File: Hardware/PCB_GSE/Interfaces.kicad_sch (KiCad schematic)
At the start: 16 parts, among them J1 GT17HN-4DP-2HA56, J15 Conn_01x02, J16 Conn_01x06_Pin, U5 ISOW1044

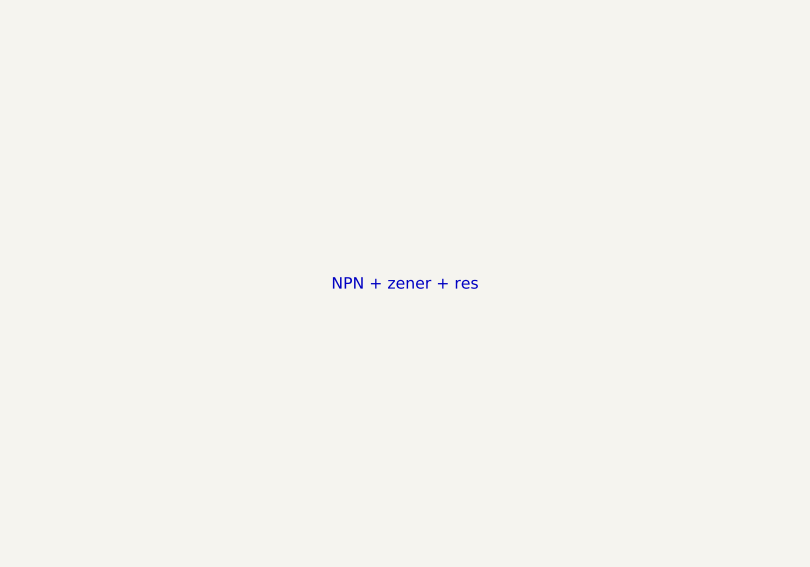
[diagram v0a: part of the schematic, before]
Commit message: fix: typos
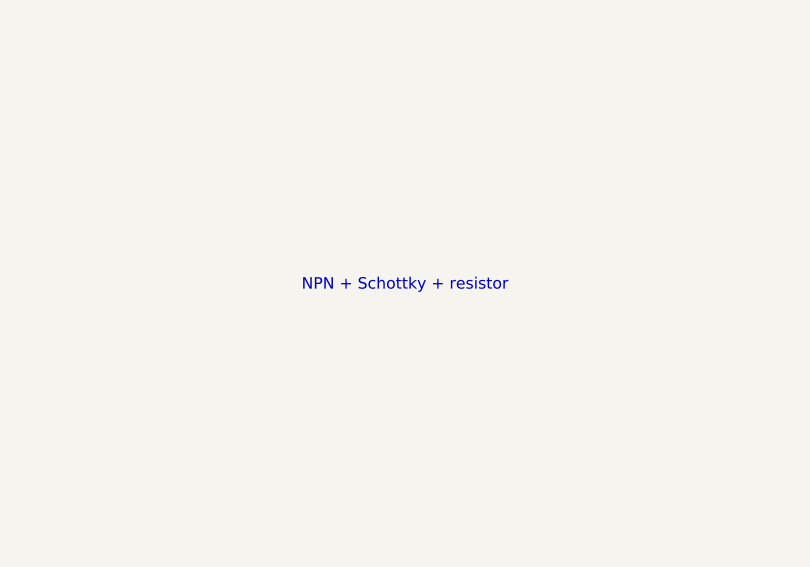
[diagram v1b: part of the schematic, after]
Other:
- note added: "NPN + Schottky + resistor"
- note removed: "NPN + zener + res"
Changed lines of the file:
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@@
 		)
 	)
-	(text "NPN + zener + res"
+	(text "NPN + Schottky + resistor"
 		(exclude_from_sim no)
 		(at 79.248 68.834 0)

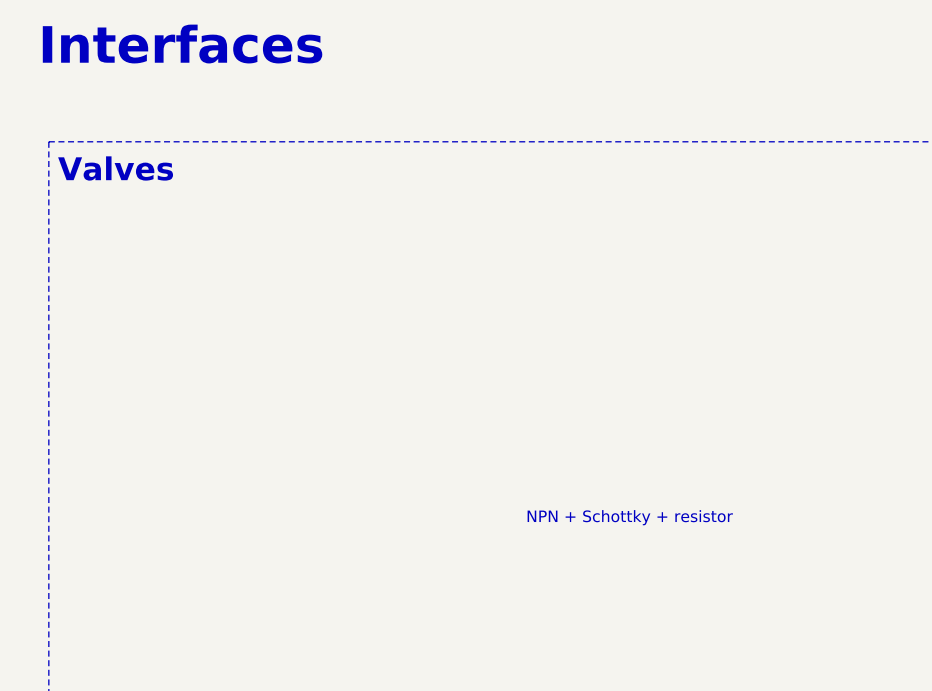
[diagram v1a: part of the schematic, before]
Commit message: fix: change Schottky diode 12v buck
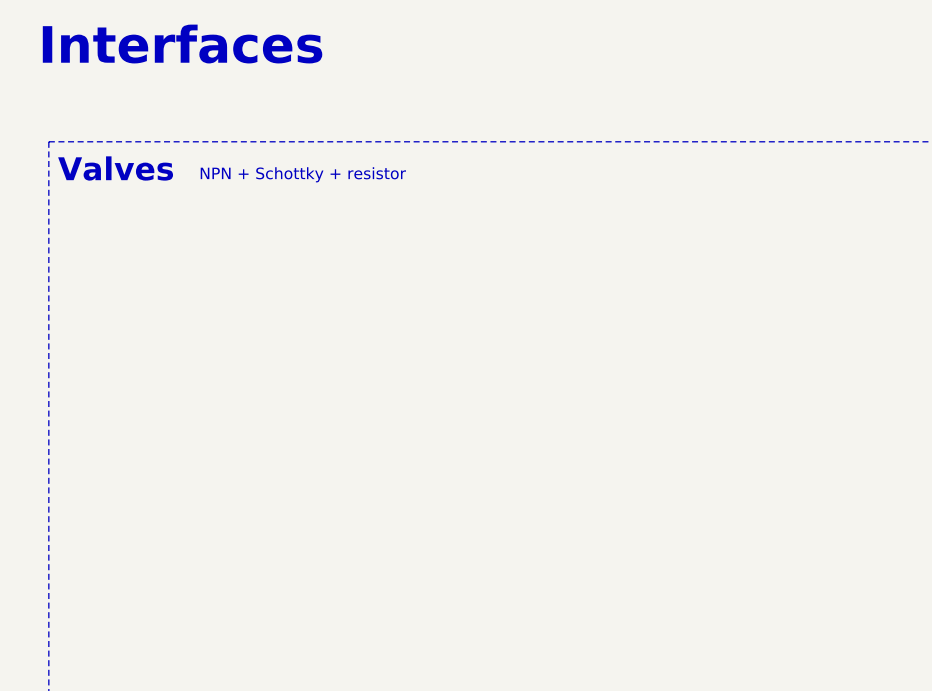
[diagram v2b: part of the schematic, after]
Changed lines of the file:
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@@
 	(text "NPN + Schottky + resistor"
 		(exclude_from_sim no)
-		(at 79.248 68.834 0)
+		(at 42.926 30.734 0)
 		(effects
 			(font

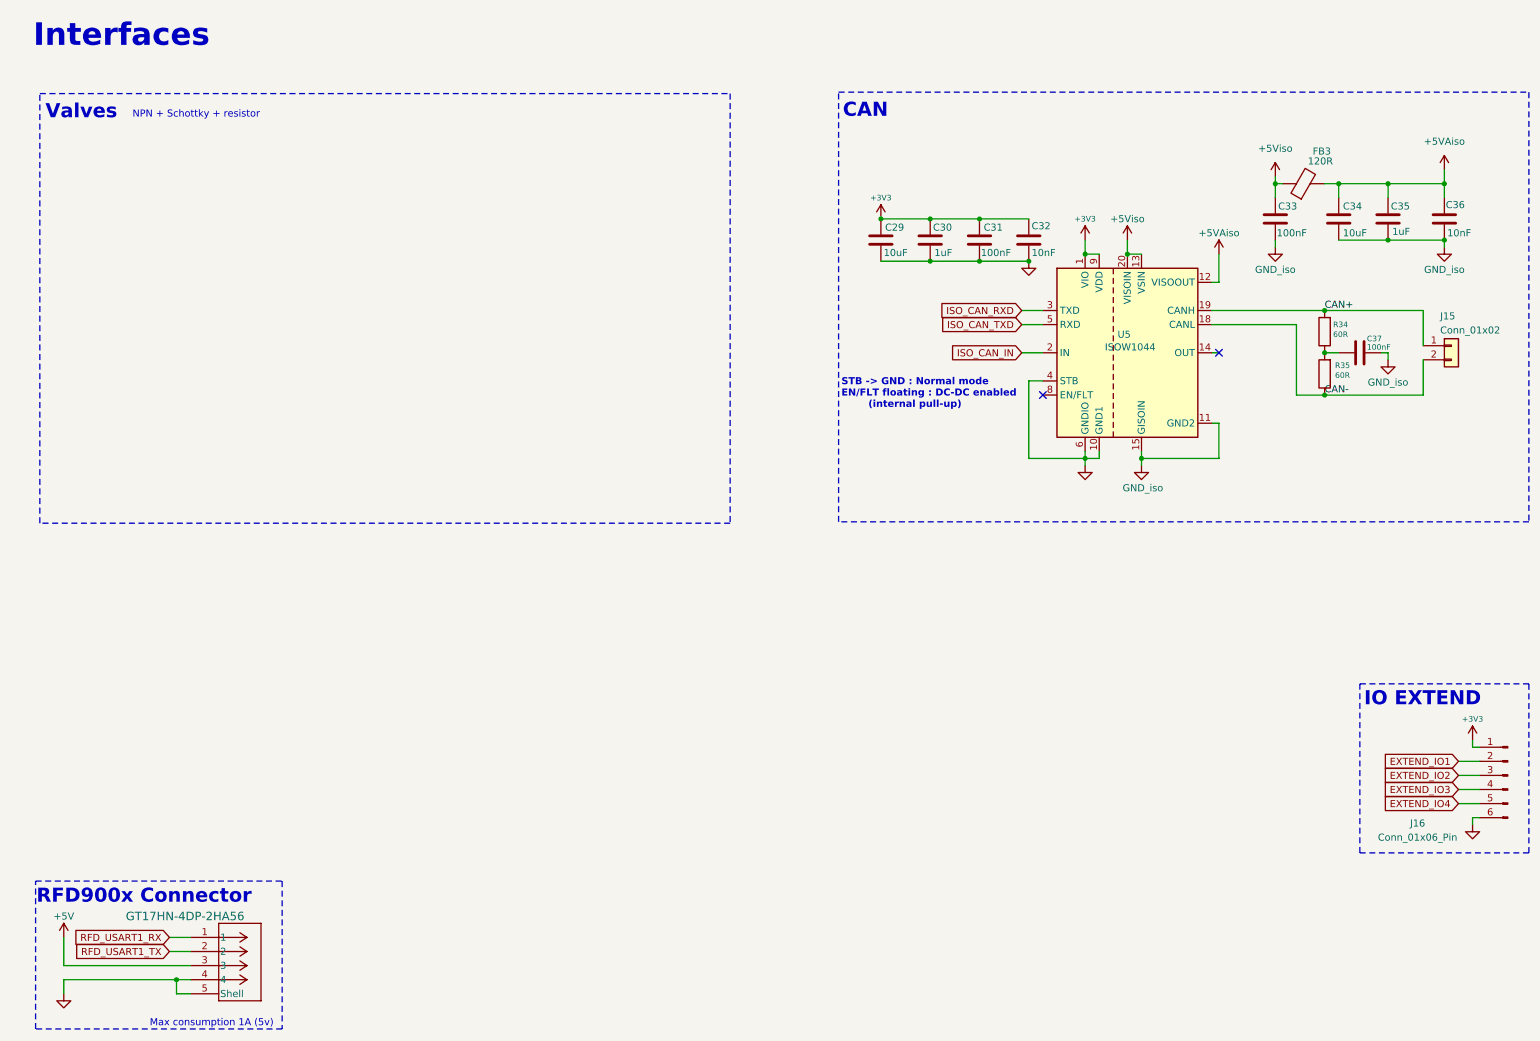
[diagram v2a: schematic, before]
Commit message: feat: add valve control + needed components
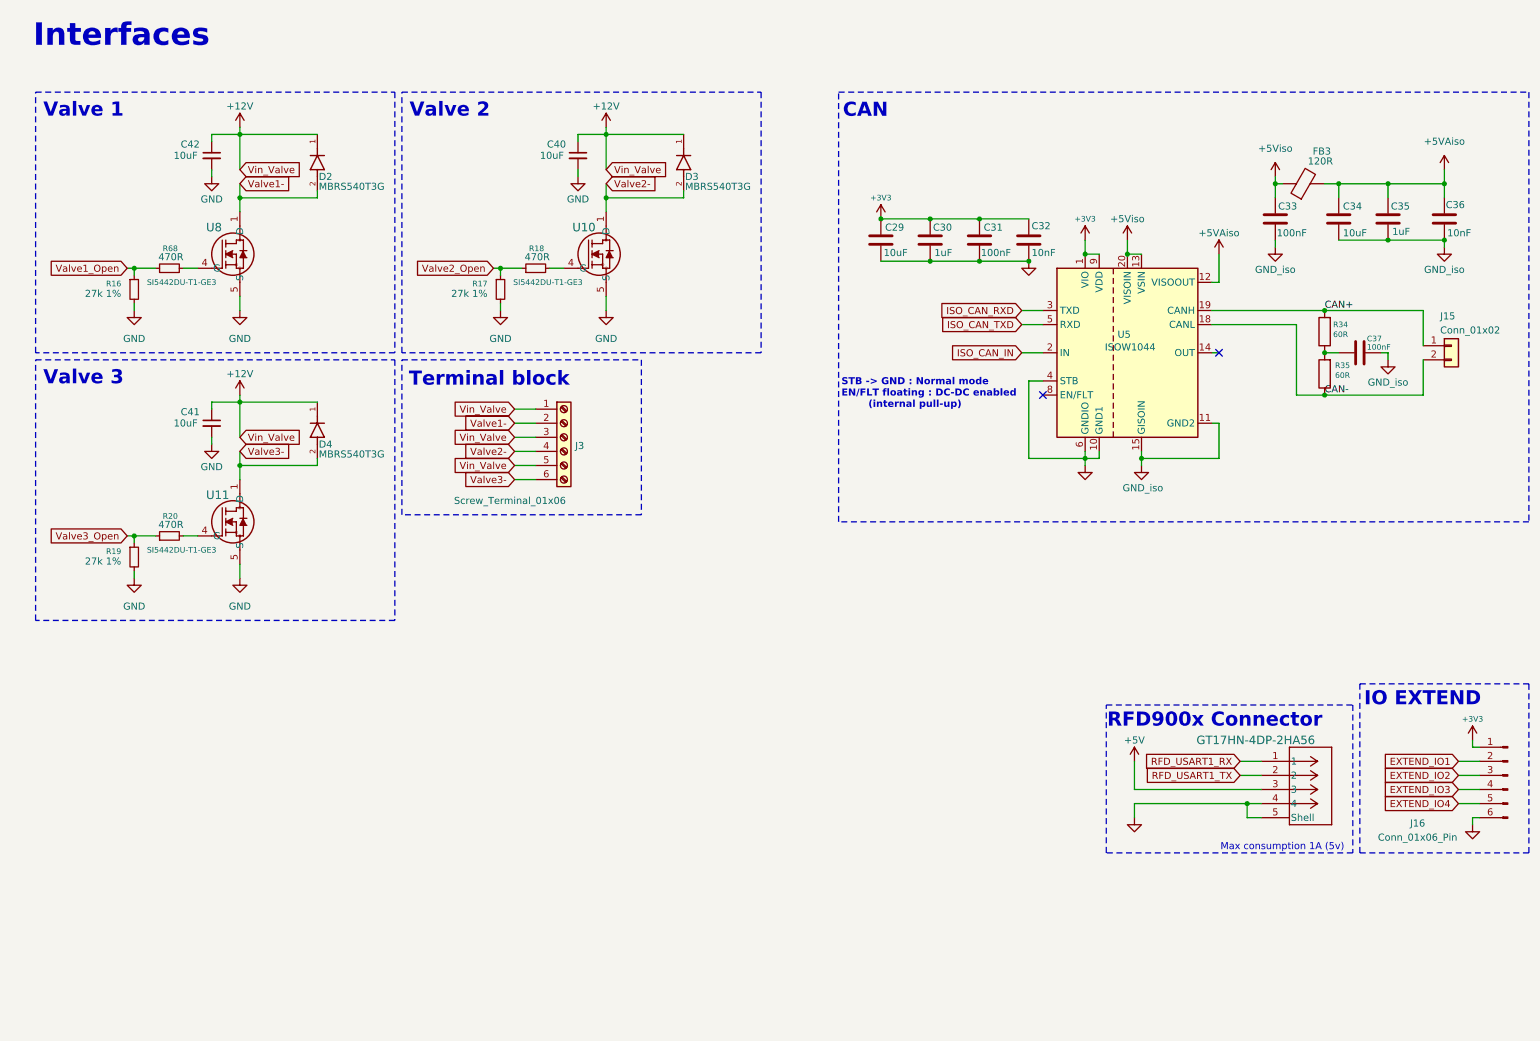
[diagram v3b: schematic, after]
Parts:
- added C40, C41, C42: 10uF, Capacitor_SMD:C_0603_1608Metric, symbol Device:C_Small
- added D2, D3, D4: MBRS540T3G, MBRS540T3G:DIOM7959X261N, symbol PCB_GSE:MBRS540T3G
- added J3: Screw_Terminal_01x06, symbol Connector:Screw_Terminal_01x06
- added R16, R17, R19: 27k 1%, Resistor_SMD:R_0603_1608Metric, symbol Device:R_Small
- added R18, R20, R68: 470R, Resistor_SMD:R_0603_1608Metric, symbol Device:R_Small
- added U10, U11, U8: SI5442DU-T1-GE3, symbol PCB_GSE:SI5442DU-T1-GE3
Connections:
- net GND: now also C40.2, C41.2, C42.2, R16.2, R17.2, R19.2, U10.5 (S), U10.9 (S), U11.5 (S), U11.9 (S), U8.5 (S), U8.9 (S)
- new net: R20.2, U11.4 (G)
- new net: R18.2, U10.4 (G)
- new net: R68.2, U8.4 (G)
- new net +12V: C40.1, C41.1, C42.1, D2.1, D3.1, D4.1, J3.1 (Pin_1), J3.3 (Pin_3), J3.5 (Pin_5)
- new net Valve1-: D2.2, J3.2 (Pin_2), U8.1 (D), U8.2 (D), U8.3 (D), U8.6 (D), U8.7 (D), U8.8 (D)
- new net Valve1_Open: R16.1, R68.1
- new net Valve2-: D3.2, J3.4 (Pin_4), U10.1 (D), U10.2 (D), U10.3 (D), U10.6 (D), U10.7 (D), U10.8 (D)
- new net Valve2_Open: R17.1, R18.1
- new net Valve3-: D4.2, J3.6 (Pin_6), U11.1 (D), U11.2 (D), U11.3 (D), U11.6 (D), U11.7 (D), U11.8 (D)
- new net Valve3_Open: R19.1, R20.1
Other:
- note added: "Terminal block"
- note added: "Valve 1"
- note added: "Valve 2"
- note added: "Valve 3"
- note removed: "NPN + Schottky + resistor"
- note removed: "Valves"

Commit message: feat: add extended ios + add stm32 project extended ios +
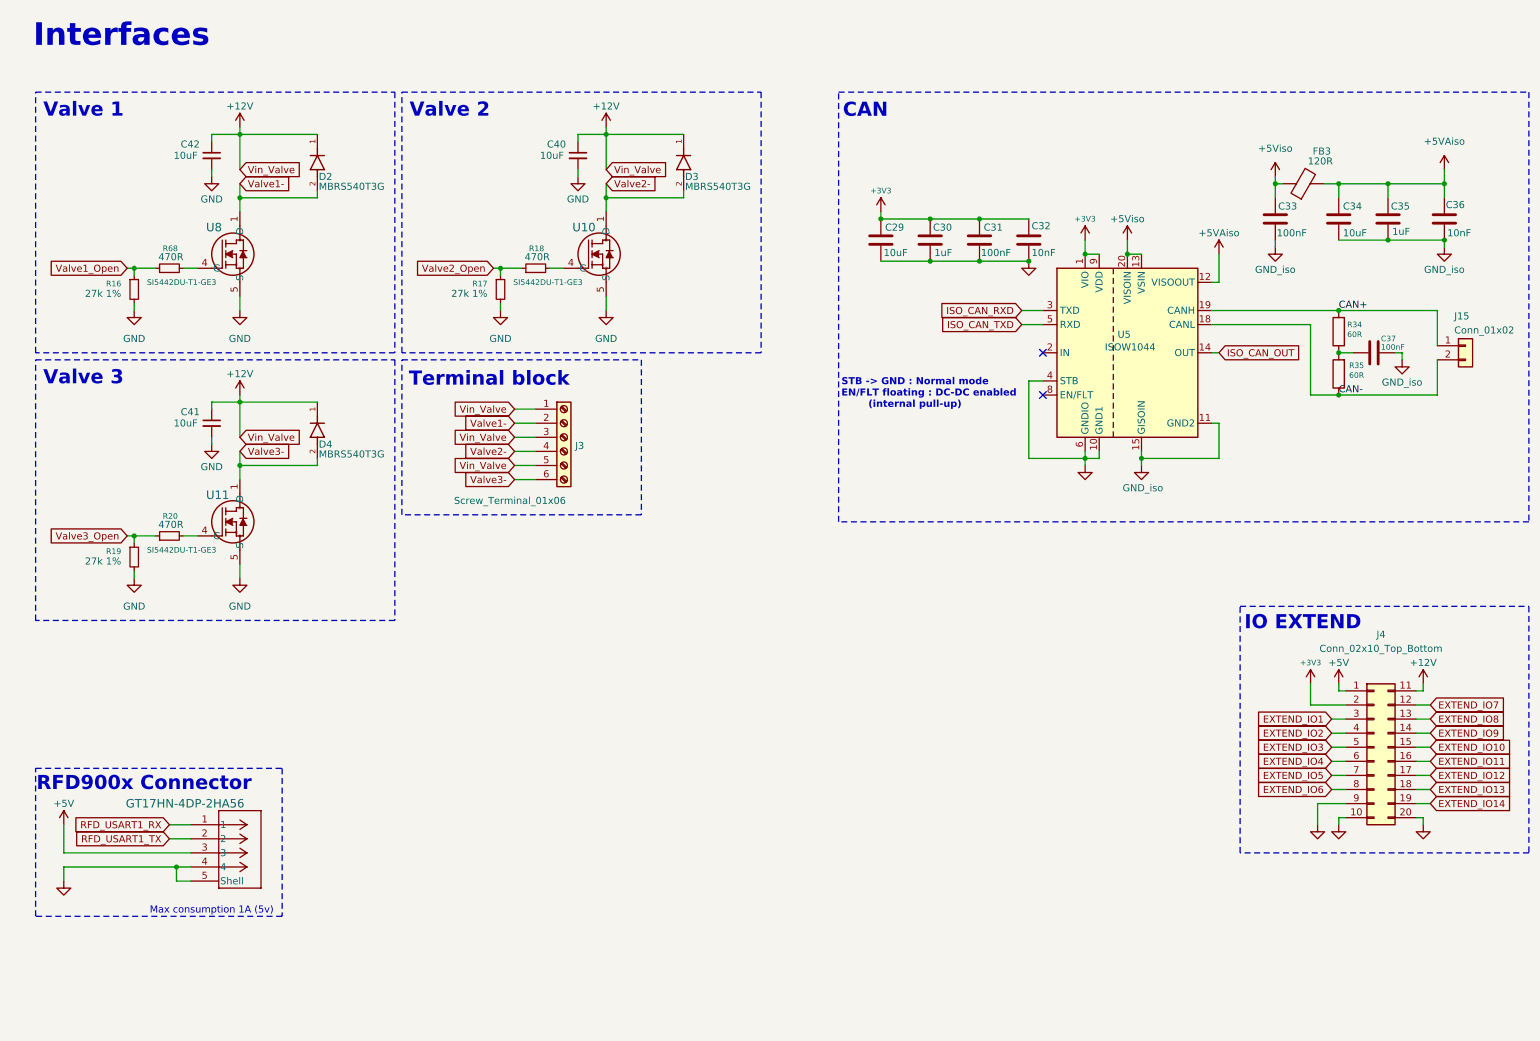
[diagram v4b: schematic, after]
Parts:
- removed J16: Conn_01x06_Pin, Connector_PinSocket_2.54mm:PinSocket_2x03_P2.54mm_Vertical, symbol Connector:Conn_01x06_Pin
- added J4: Conn_02x10_Top_Bottom, Connector_PinHeader_2.54mm:PinHeader_2x10_P2.54mm_Vertical, symbol Connector_Generic:Conn_02x10_Top_Bottom
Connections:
- net +12V: now also J4.11 (Pin_11)
- net +3V3: now also J4.2 (Pin_2)
- net +5V: now also J4.1 (Pin_1)
- net EXTEND_IO1: now also J4.3 (Pin_3)
- net EXTEND_IO2: now also J4.4 (Pin_4)
- net EXTEND_IO3: now also J4.5 (Pin_5)
- net EXTEND_IO4: now also J4.6 (Pin_6)
- net GND: now also J4.10 (Pin_10), J4.20 (Pin_20), J4.9 (Pin_9)
- net ISO_CAN_OUT: now reaches U5.14 (OUT)
- net ISO_CAN_IN: no longer names the net of U5.2 (IN)
- new net EXTEND_IO10: J4.15 (Pin_15)
- new net EXTEND_IO11: J4.16 (Pin_16)
- new net EXTEND_IO12: J4.17 (Pin_17)
- new net EXTEND_IO13: J4.18 (Pin_18)
- new net EXTEND_IO14: J4.19 (Pin_19)
- new net EXTEND_IO5: J4.7 (Pin_7)
- new net EXTEND_IO6: J4.8 (Pin_8)
- new net EXTEND_IO7: J4.12 (Pin_12)
- new net EXTEND_IO8: J4.13 (Pin_13)
- new net EXTEND_IO9: J4.14 (Pin_14)
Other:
- moved on the sheet: C37, J15, R34, R35

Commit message: refactor: merge emile + main branches
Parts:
- renumbered C42 to C36, C41 to C37, C40 to C38, C29 to C39, C30 to C40, C31 to C41, C32 to C42, C33 to C43, C34 to C44, C37 to C45, C35 to C46, C36 to C47, D4 to D3, D3 to D4, FB3 to FB4, J1 to J3, J3 to J4, J4 to J5, J15 to J6, R16 to R25, R19 to R26, R68 to R27, R20 to R28, R17 to R29, R18 to R30, R34 to R31, R35 to R32, U8 to U5, U11 to U6, U10 to U7, U5 to U8
